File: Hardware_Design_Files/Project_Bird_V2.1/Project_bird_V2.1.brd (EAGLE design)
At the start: 85.5 x 20 mm, 55 parts, among them U1 MS560702BA03-50, U10 MGSF2N02EL, U2 SST26VF032B-104I/SM, U3 LIS331DLHTR, U4 ZLDO1117G33TA, U5 MGSF2N02EL, U6 MGSF2N02EL, U7 MGSF2N02EL, U8 MGSF2N02EL, U9 ATMEGA32U4-AU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

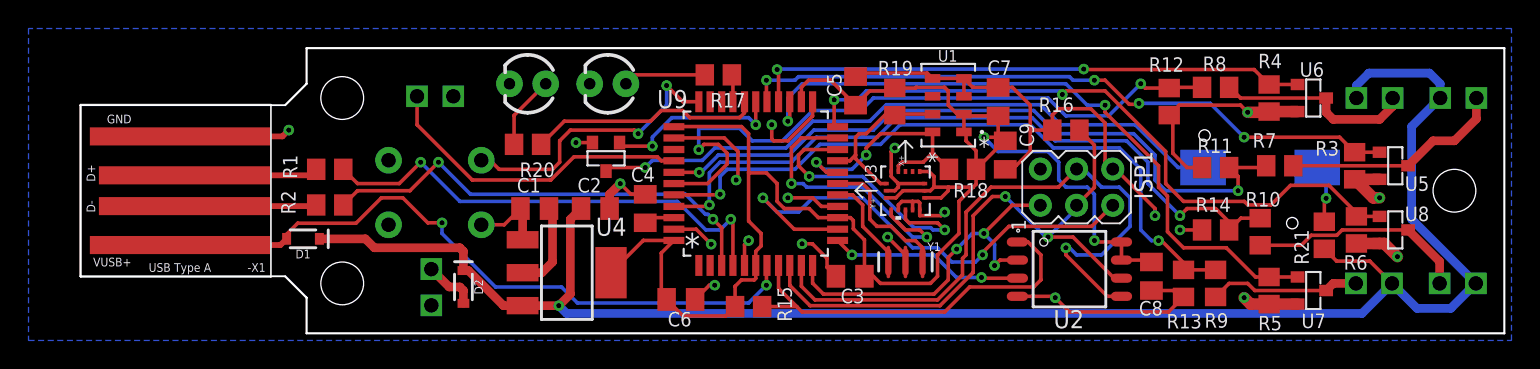
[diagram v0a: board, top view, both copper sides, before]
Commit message: Created Flight Recorder Library to handle flight stats and flash recording.
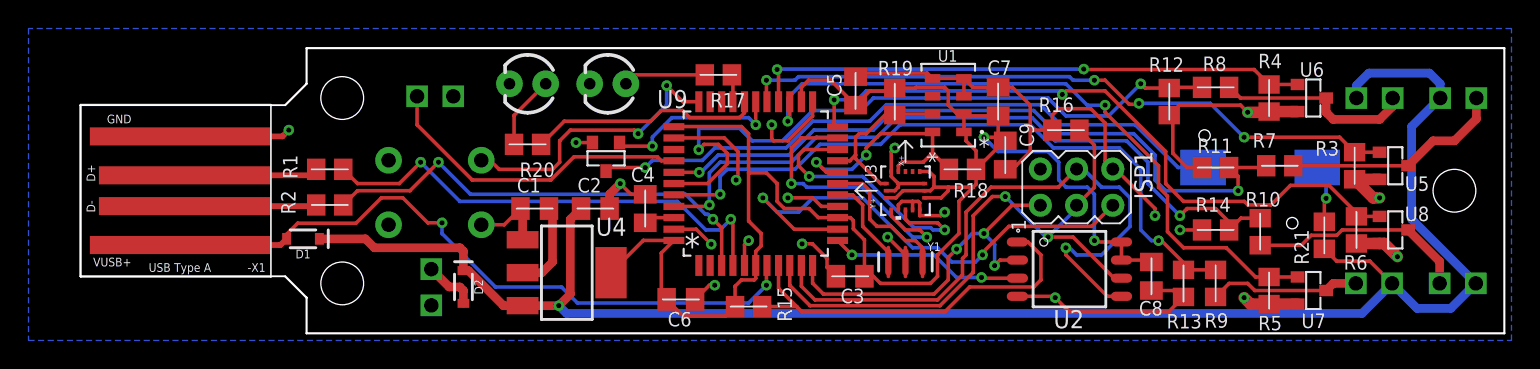
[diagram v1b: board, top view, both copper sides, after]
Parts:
- J1, J2, J3, J4, J5, J6: device SparkFun-Connectors:1X02_2.54_SCREWTERM -> UTS_Rocketry_Main_EAGLE_Library:1X02_2.54_SCREWTERM

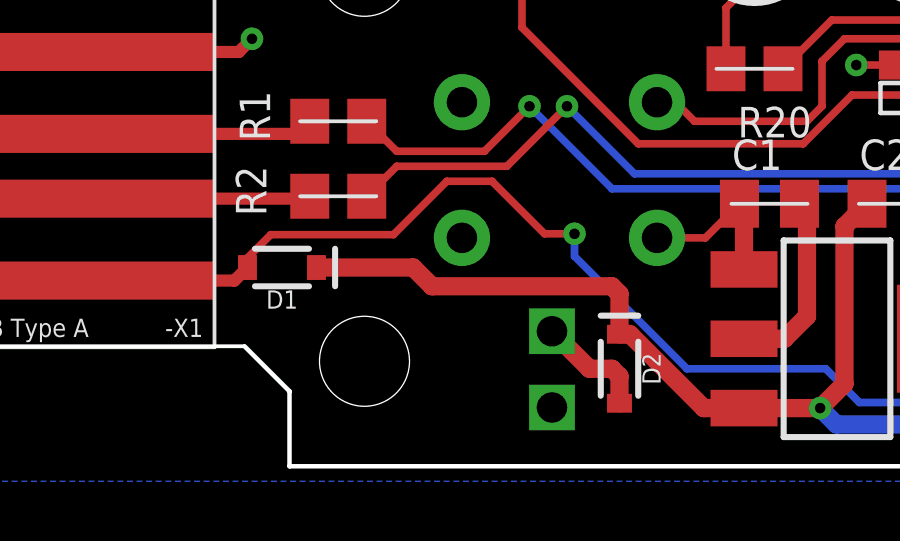
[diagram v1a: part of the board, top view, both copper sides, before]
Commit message: Reduced Program Size and Fixed Hardware 3D CAD
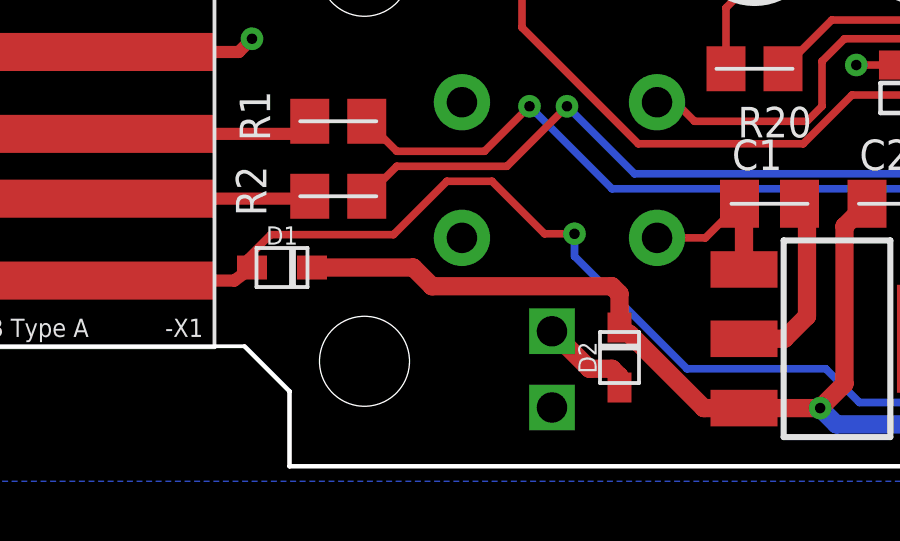
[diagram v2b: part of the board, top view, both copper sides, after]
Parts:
- D1, D2: device SparkFun-DiscreteSemi:SOD-323 -> UTS_Rocketry_Main_EAGLE_Library:SOD-323F
- D3, D4: device SparkFun-LED:LED_3MM -> UTS_Rocketry_Main_EAGLE_Library:LED_3MM
- ISP1: device adafruit:AVRISP -> UTS_Rocketry_Main_EAGLE_Library:AVRISP
- S1: value MOMENTARY-SWITCH-SPST-PTH-6.0MM -> MOMENTARY-SWITCH-SPST; device SparkFun-Switches:TACTILE_SWITCH_PTH_6.0MM -> UTS_Rocketry_Main_EAGLE_Library:TACTILE_SWITCH_PTH_6.0MM
- moved D2 0.38 mm to (11.0, 3.62), turned to 90 degrees
- turned D1 to 0 degrees
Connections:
- net BUTTON: now also S1.2
- net GND: now also S1.4
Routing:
- net N$1: track 3.77 -> 3.25 mm
